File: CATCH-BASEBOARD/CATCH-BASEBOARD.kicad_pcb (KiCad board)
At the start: 2 copper layers, 100 x 60 mm, 17 parts, among them J1 SJ3-35083B-TR, J2 Conn_02x04_Odd_Even, SW1 SW_SPST, U1 PC817, U2 TPS22918DBVR, U3 DMG2305UX-13

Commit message: First Layout Revision
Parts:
- moved R4 179.6 mm to (258.8, 68.0), turned to -90 degrees
- moved R3 149.9 mm to (218.9, 57.1), turned to 90 degrees
- moved R2 147.3 mm to (207.0, 43.2)
- moved C3 146.0 mm to (263.5, 61.1)
- moved U2 143.8 mm to (210.7, 57.7), turned to 180 degrees
- moved SW1 142.8 mm to (266.1, 74.0), turned to 90 degrees
- moved TP2 142.2 mm to (274.2, 76.8)
- moved R1 141.4 mm to (222.8, 69.8), turned to 180 degrees
- moved TP1 138.2 mm to (269.9, 77.0)
- moved J2 136.9 mm to (193.7, 41.1)
- moved U3 132.7 mm to (252.7, 72.5), turned to 90 degrees
- moved JP1 127.8 mm to (252.7, 69.2), turned to 0 degrees
- moved C2 100.5 mm to (211.6, 61.4), turned to -90 degrees
- moved C1 94.3 mm to (206.4, 60.8), turned to 90 degrees
- moved U1 82.7 mm to (202.2, 37.3), turned to 90 degrees
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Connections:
- J2 pad 5: SDA -> SCL
- J2 pad 7: SCL -> SDA
- U1 pad 1: Net-(R2-Pad1) -> JACK_LEFT
- U1 pad 2: GND -> JACK MIDDLE
- U1 pad 3: JACK MIDDLE -> GND
- U1 pad 4: JACK_LEFT -> Net-(R2-Pad1)
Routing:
- net INTERRUPT/PWM1: track 0.00 -> 89.5 mm
- net SDA: track 0.00 -> 76.4 mm
- net SCL: track 0.00 -> 73.2 mm
- net R_ID_PIN: track 0.00 -> 72.5 mm
- net ADC0: track 0.00 -> 66.4 mm
- net Net-(A1-GPIO28_ADC2): track 0.00 -> 42.7 mm
- net GPIO13: track 0.00 -> 41.2 mm
- net VUSB: track 0.00 -> 33.4 mm
- net OUTPUT3.3: track 0.00 -> 30.3 mm
- net GPIO12: track 0.00 -> 29.5 mm
- net GND: track 0.00 -> 28.3 mm
- net Net-(JP1-B): track 0.00 -> 16.2 mm
- net JACK MIDDLE: track 0.00 -> 14.0 mm
- net JACK_LEFT: track 0.00 -> 12.8 mm
- net Net-(SW1-A): track 0.00 -> 9.97 mm
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- added copper zone on B.Cu, net GND

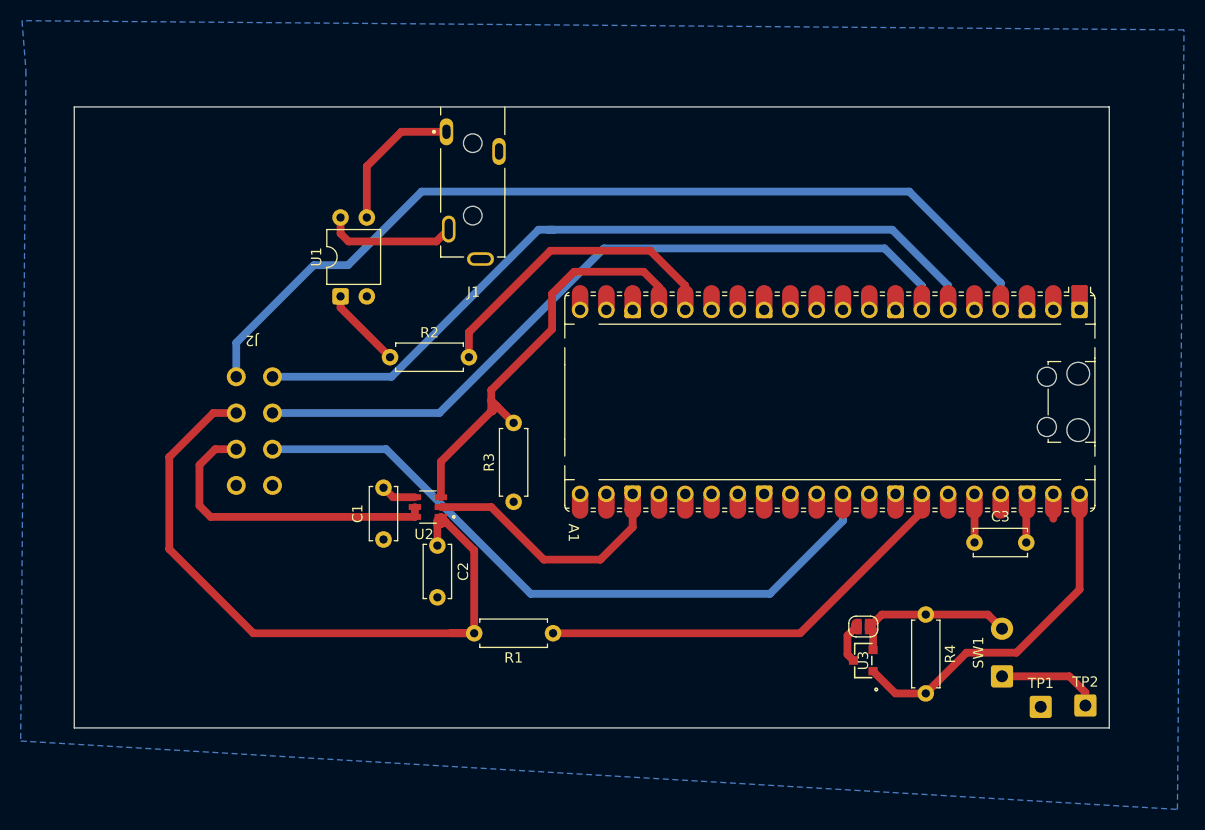
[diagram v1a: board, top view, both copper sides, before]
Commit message: Fixed Schematic + Finished Layout v.1
Layout still needs some touching up on, especially vias. I'll be changing it to fix all the errors on the DRC.
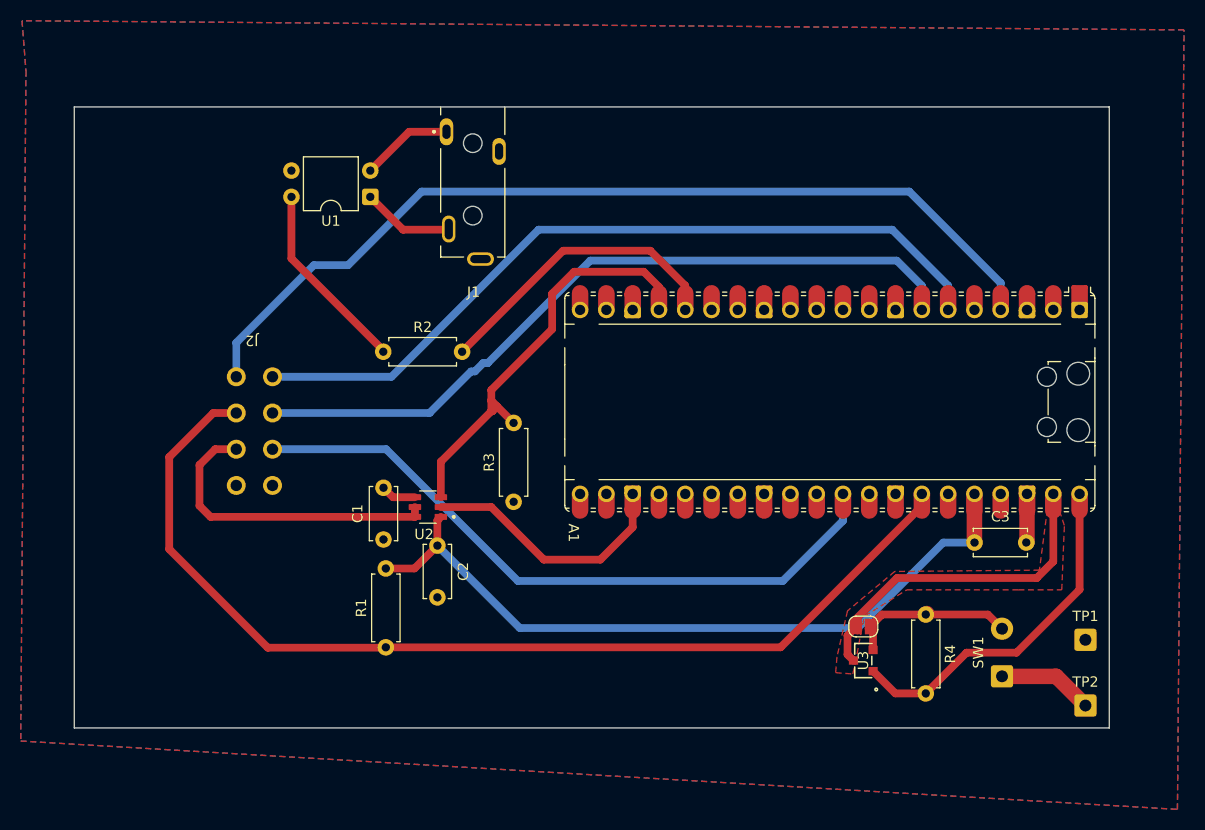
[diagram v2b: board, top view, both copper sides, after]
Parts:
- moved R1 16.2 mm to (206.6, 71.2), turned to 90 degrees
- moved U1 10.0 mm to (205.1, 27.7), turned to 180 degrees
- moved TP1 7.78 mm to (274.2, 70.5)
- moved R2 0.85 mm to (206.3, 42.6)
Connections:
- A1 pad 34: Net-(A1-GPIO28_ADC2) -> R_ID_PIN
- A1 pad 36: R_ID_PIN -> +3V3
- C2 pad 1: R_ID_PIN -> +3V3
- C3 pad 1: R_ID_PIN -> +3V3
- R1 pad 1: Net-(A1-GPIO28_ADC2) -> R_ID_PIN
- R1 pad 2: R_ID_PIN -> +3V3
- U2 pad 1: R_ID_PIN -> +3V3
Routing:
- net +3V3: track 0.00 -> 72.1 mm
- net Net-(A1-GPIO28_ADC2): track 42.7 -> 0.00 mm
- net R_ID_PIN: track 72.5 -> 101.1 mm
- net VSYS: track 5.49 -> 32.1 mm
- net Net-(R2-Pad1): track 7.86 -> 18.6 mm
- net JACK MIDDLE: track 14.0 -> 8.91 mm
- net JACK_LEFT: track 12.8 -> 8.92 mm
- net ADC0: track 66.4 -> 65.4 mm
- net SCL: track 73.2 -> 72.2 mm
- net GPIO12: track 29.5 -> 28.5 mm
- net GND: track 28.3 -> 29.2 mm, vias 0 -> 241
- net Net-(SW1-A): track 9.97 -> 9.23 mm
- net SDA: track 76.4 -> 75.7 mm
- added copper zone on F.Cu, net GND
- added copper zone on F.Cu, net VSYS
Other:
- board text added: "Copper"
- board text added: "Exposed"
- board text added: "Keep Out"
- board text added: "PCB EDGE"
- board text added: "USB Cable"

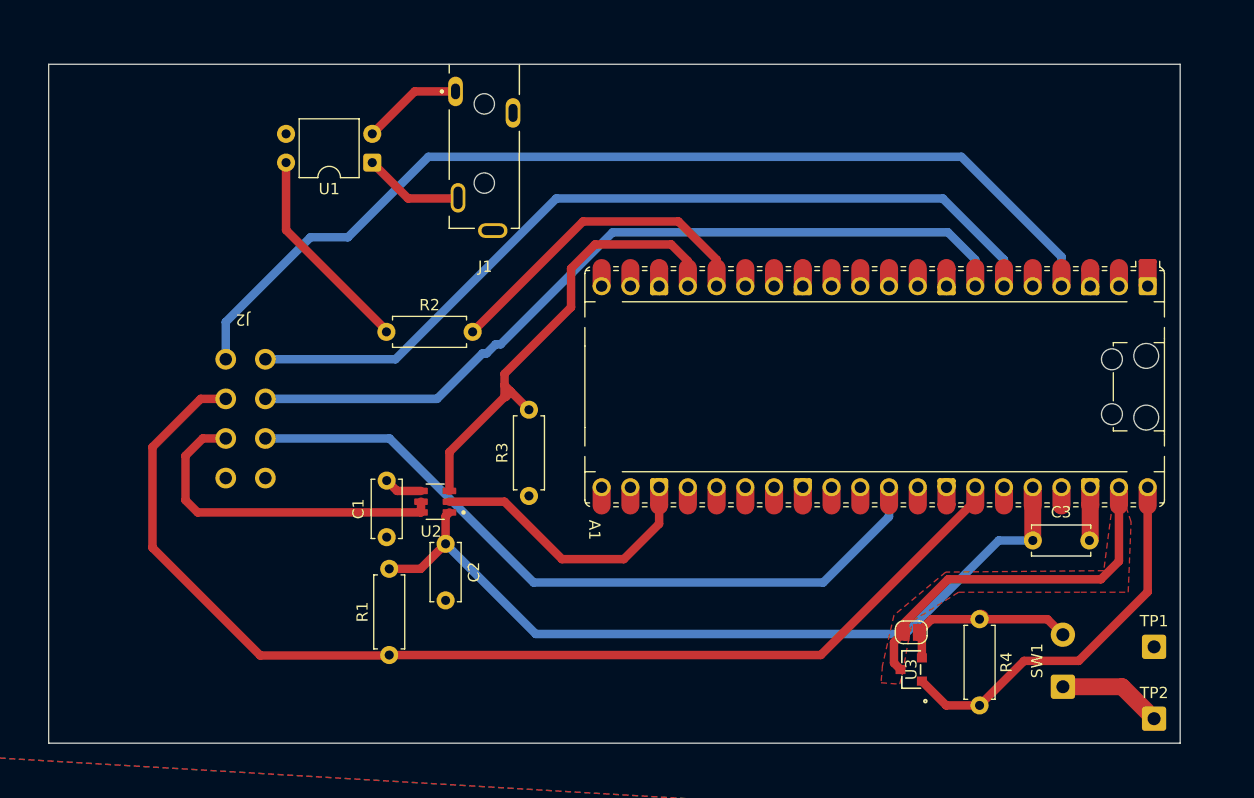
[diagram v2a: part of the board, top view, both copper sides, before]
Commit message: Finished PCB
Fixed some layout, added on board documentation.
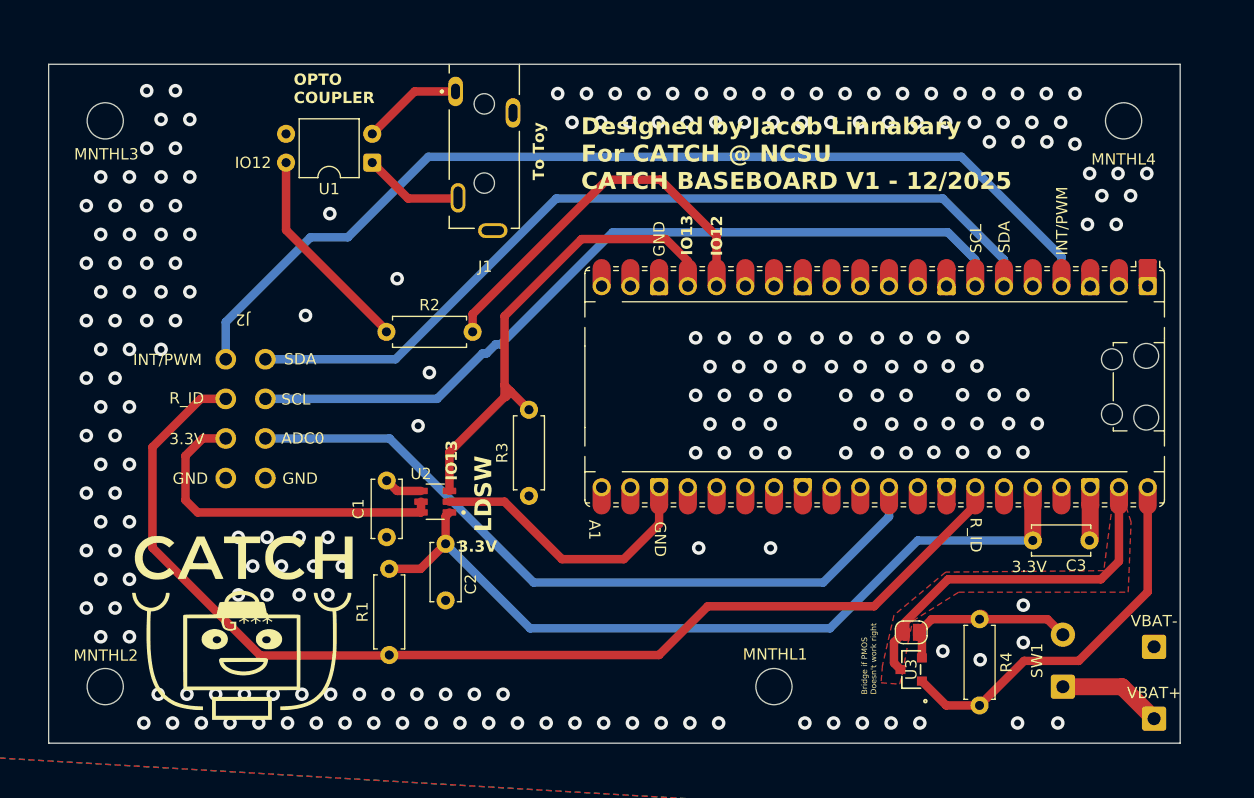
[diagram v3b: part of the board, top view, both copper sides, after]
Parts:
- added G***: LOGO, LOGO, F.Cu at (194.0, 68.3)
- added MNTHL1: MountingHole_3.2mm_M3, MountingHole:MountingHole_3.2mm_M3, F.Cu at (240.6, 74.0)
- added MNTHL2: MountingHole_3.2mm_M3, MountingHole:MountingHole_3.2mm_M3, F.Cu at (181.5, 74.0)
- added MNTHL3: MountingHole_3.2mm_M3, MountingHole:MountingHole_3.2mm_M3, F.Cu at (181.5, 24.0)
- added MNTHL4: MountingHole_3.2mm_M3, MountingHole:MountingHole_3.2mm_M3, F.Cu at (271.5, 24.0)
- renumbered TP2 to VBAT+, TP1 to VBAT-
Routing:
- net GPIO12: track 28.5 -> 33.7 mm
- net GPIO13: track 41.2 -> 42.5 mm
- net GND: vias 241 -> 216
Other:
- board text added: "3.3V"
- board text added: "ADC0"
- board text added: "Bridge if PMOS Doesn't work right"
- board text added: "Designed by Jacob Linnabary For CATCH @ NCSU CATCH BASEBOARD V1 - 12/2025"
- board text added: "GND"
- board text added: "INT/PWM"
- board text added: "IO12"
- board text added: "IO13"
- board text added: "LDSW"
- board text added: "OPTO COUPLER"
- board text added: "R_ID"
- board text added: "SCL"
- board text added: "SDA"
- board text added: "To Toy"
